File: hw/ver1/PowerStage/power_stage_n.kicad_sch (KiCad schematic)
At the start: 14 parts, among them Q2 Q_NMOS_DGS, Q6 Q_NMOS_DGS, U5 LTC7060

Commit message: Sync wip
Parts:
- removed D1: D_Schottky, symbol Device:D_Schottky
- removed Q2, Q6: Q_NMOS_DGS, symbol Device:Q_NMOS_DGS
- added D5: SS210, Diode_SMD:D_SMA, symbol Diode:SS210
- added Q10, Q2: MCAC80N10Y, Project Mosfets:TRANS_BSC076N06NS3-G, symbol ProjectMosfets:MCAC80N10Y
- C41: value C -> 200nF
- C45: value C -> 330nF
- L1: value L_Ferrite -> 3.3uH; Digikey (none) -> PQ2614BLA-3R3K-ND
- R53, R57: value R_US -> 10k
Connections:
- net GND: now also Q2.3 (S)
- net VCC: now also D5.2 (A)
- net VHIGH: now also Q10.1 (D)
- net at C11.2, L1.1, R53.1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: now also Q10.3 (S), Q2.1 (D)
- net at U5.11 (TG): now also Q10.2 (G)
- net at C11.1, U5.12 (BST): now also D5.1 (K)
- net at U5.8 (BG): now also Q2.2 (G)
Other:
- note added: "These components are sized to peak current load at 12v design limit from ltc7871.ipynb. Still need to validate other configurations."
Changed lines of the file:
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@@
+	)
+	(junction
+		(at 168.91 88.9)
+		(diameter 0)
+		(color 0 0 0 0)
 	)
 	(junction
@@
 		(color 0 0 0 0)
 	)
-	(junction
-		(at 168.91 88.9)
-		(diameter 0)
-		(color 0 0 0 0)
-	)
 	(no_connect
 		(at 133.35 76.2)
@@
 			(width 0)
 			(type default)
+		)
+	)
+	(text "These components are sized to peak current load at 12v design limit from ltc7871.ipynb.\nStill need to validate other configurations."
+		(exclude_from_sim no)
+		(at 169.926 37.846 0)
+		(effects
+			(font
+				(size 1.27 1.27)
+			)
 		)
 	)
@@
 			)
 		)
-		(property "Value" "L_Ferrite"
+		(property "Value" "3.3uH"
 			(at 193.04 79.248 90)
 			(effects
@@
 			)
 		)
-		(property "Datasheet" "~"
+		(property "Datasheet" "https://www.bourns.com/docs/Product-Datasheets/PQ2614.pdf"
 			(at 193.04 77.47 0)
 			(effects
@@
 		(property "Description" "Inductor with ferrite core"
 			(at 193.04 77.47 0)
+			(effects
+				(font
+					(size 1.27 1.27)
+				)
+				(hide yes)
+			)
+		)
+		(property "Digikey" "PQ2614BLA-3R3K-ND"
+			(at 193.548 81.28 90)
 			(effects
 				(font
@@
 	)
 	(symbol
-		(lib_id "Device:Q_NMOS_DGS")
-		(at 166.37 83.82 0)
+		(lib_id "ProjectMosfets:MCAC80N10Y")
+		(at 166.37 71.12 0)
 		(unit 1)
 		(exclude_from_sim no)
@@
 		(dnp no)
 		(fields_autoplaced yes)
-		(property "Reference" "Q6"
-			(at 172.72 82.5499 0)
+		(property "Reference" "Q10"
+			(at 172.72 69.8499 0)
 			(effects
 				(font
@@
 			)
 		)
-		(property "Value" "Q_NMOS_DGS"
-			(at 172.72 85.0899 0)
+		(property "Value" "MCAC80N10Y"
+			(at 172.72 72.3899 0)
 			(effects
 				(font
@@
 			)
 		)
-		(property "Footprint" ""
-			(at 171.45 81.28 0)
-			(effects
-				(font
-					(size 1.27 1.27)
-				)
-				(hide yes)
-			)
-		)
-		(property "Datasheet" "~"
-			(at 166.37 83.82 0)
+		(property "Footprint" "Project Mosfets:TRANS_BSC076N06NS3-G"
+			(at 171.45 68.58 0)
+			(effects
+				(font
+					(size 1.27 1.27)
+				)
+				(hide yes)
+			)
+		)
+		(property "Datasheet" "https://www.mccsemi.com/pdf/Products/MCAC80N10Y(DFN5060).pdf"
+			(at 166.37 71.12 0)
 			(effects
 				(font
@@
 		)
 		(property "Description" "N-MOSFET transistor, drain/gate/source"
-			(at 166.37 83.82 0)
+			(at 166.37 71.12 0)
+			(effects
+				(font
+					(size 1.27 1.27)
+				)
+				(hide yes)
+			)
+		)
+		(property "DigiKey" "353-MCAC80N10Y-TPCT-ND"
+			(at 166.37 71.12 0)
 			(effects
 				(font
@@
 		(pin "1"
 		)
+		(pin "2"
+		)
 		(pin "3"
-		)
-		(pin "2"
 		)
 		(instances
 			(project "IchnaeaV1"
 				(path "/1a8ad36a-4b76-4949-97c2-661f12a0b1d9/2acacade-9567-40f5-9827-bf22bd24fca6/ec98a9c6-939d-4e77-a0cb-de9e7d256244"
-					(reference "Q6")
+					(reference "Q10")
 					(unit 1)
 				)
 				(path "/1a8ad36a-4b76-4949-97c2-661f12a0b1d9/2acacade-9567-40f5-9827-bf22bd24fca6/fa9aff26-caf6-491a-a4dd-20eb067f1f07"
-					(reference "Q7")
+					(reference "Q11")
 					(unit 1)
 				)
 				(path "/1a8ad36a-4b76-4949-97c2-661f12a0b1d9/2acacade-9567-40f5-9827-bf22bd24fca6/9404991a-84cd-40d3-b41e-b6fd90033c77"
-					(reference "Q8")
+					(reference "Q12")
 					(unit 1)
 				)
 				(path "/1a8ad36a-4b76-4949-97c2-661f12a0b1d9/2acacade-9567-40f5-9827-bf22bd24fca6/951e871e-184d-412d-983e-cb08401577f3"
-					(reference "Q9")
+					(reference "Q13")
 					(unit 1)
 				)
@@
 			)
 		)
-		(property "Value" "R_US"
+		(property "Value" "10k"
 			(at 196.85 60.9599 0)
 			(effects
@@
 			)
 		)
-		(property "Value" "R_US"
+		(property "Value" "10k"
 			(at 180.34 60.96 90)
 			(effects
@@
 	)
 	(symbol
-		(lib_id "Device:C")
-		(at 185.42 54.61 0)
+		(lib_id "Diode:SS210")
+		(at 142.24 57.15 180)
 		(unit 1)
 		(exclude_from_sim no)
@@
 		(dnp no)
 		(fields_autoplaced yes)
+		(property "Reference" "D5"
+			(at 142.5575 50.8 0)
+			(effects
+				(font
+					(size 1.27 1.27)
+				)
+			)
+		)
+		(property "Value" "SS210"
+			(at 142.5575 53.34 0)
+			(effects
+				(font
+					(size 1.27 1.27)
+				)
+			)
+		)
+		(property "Footprint" "Diode_SMD:D_SMA"
+			(at 142.24 52.705 0)
+			(effects
+				(font
+					(size 1.27 1.27)
+				)
+				(hide yes)
+			)
+		)
+		(property "Datasheet" "https://www.wontop.com/uploadfiles/56/sort_excel/pdf/ss22.pdf"
+			(at 142.24 57.15 0)
+			(effects
+				(font
+					(size 1.27 1.27)
+				)
+				(hide yes)
+			)
+		)
+		(property "Description" "100V 2A Schottky Diode, SMA"
+			(at 142.24 57.15 0)
+			(effects
+				(font
+					(size 1.27 1.27)
+				)
+				(hide yes)
+			)
+		)
+		(property "LCSC" "C14996"
+			(at 142.24 57.15 0)
+			(effects
+				(font
+					(size 1.27 1.27)
+				)
+				(hide yes)
+			)
+		)
+		(pin "2"
+		)
+		(pin "1"
+		)
+		(instances
+			(project "IchnaeaV1"
+				(path "/1a8ad36a-4b76-4949-97c2-661f12a0b1d9/2acacade-9567-40f5-9827-bf22bd24fca6/ec98a9c6-939d-4e77-a0cb-de9e7d256244"
+					(reference "D5")
+					(unit 1)
+				)
+				(path "/1a8ad36a-4b76-4949-97c2-661f12a0b1d9/2acacade-9567-40f5-9827-bf22bd24fca6/fa9aff26-caf6-491a-a4dd-20eb067f1f07"
+					(reference "D6")
+					(unit 1)
+				)
+				(path "/1a8ad36a-4b76-4949-97c2-661f12a0b1d9/2acacade-9567-40f5-9827-bf22bd24fca6/9404991a-84cd-40d3-b41e-b6fd90033c77"
+					(reference "D7")
+					(unit 1)
+				)
+				(path "/1a8ad36a-4b76-4949-97c2-661f12a0b1d9/2acacade-9567-40f5-9827-bf22bd24fca6/951e871e-184d-412d-983e-cb08401577f3"
+					(reference "D8")
+					(unit 1)
+				)
+			)
+		)
+	)
+	(symbol
+		(lib_id "Device:C")
+		(at 185.42 54.61 0)
+		(mirror y)
+		(unit 1)
+		(exclude_from_sim no)
+		(in_bom yes)
+		(on_board yes)
+		(dnp no)
 		(property "Reference" "C41"
-			(at 189.23 53.3399 0)
+			(at 181.61 53.3399 0)
 			(effects
 				(font
@@
 			)
 		)
-		(property "Value" "C"
-			(at 189.23 55.8799 0)
+		(property "Value" "200nF"
+			(at 181.61 55.8799 0)
 			(effects
 				(font
@@
 		)
 		(property "Footprint" ""
-			(at 186.3852 58.42 0)
+			(at 184.4548 58.42 0)
 			(effects
 				(font
@@
 			)
 		)
-		(property "Value" "C"
+		(property "Value" "330nF"
 			(at 198.12 50.7999 0)
 			(effects
@@
 	)
 	(symbol
-		(lib_id "Device:D_Schottky")
-		(at 142.24 57.15 180)
-		(unit 1)
-		(exclude_from_sim no)
-		(in_bom yes)
-		(on_board yes)
-		(dnp no)
-		(fields_autoplaced yes)
-		(property "Reference" "D1"
-			(at 142.5575 50.8 0)
-			(effects
-				(font
-					(size 1.27 1.27)
-				)
-			)
-		)
-		(property "Value" "D_Schottky"
-			(at 142.5575 53.34 0)
-			(effects
-				(font
-					(size 1.27 1.27)
-				)
-			)
-		)
-		(property "Footprint" ""
-			(at 142.24 57.15 0)
-			(effects
-				(font
-					(size 1.27 1.27)
-				)
-				(hide yes)
-			)
-		)
-		(property "Datasheet" "~"
-			(at 142.24 57.15 0)
-			(effects
-				(font
-					(size 1.27 1.27)
-				)
-				(hide yes)
-			)
-		)
-		(property "Description" "Schottky diode"
-			(at 142.24 57.15 0)
-			(effects
-				(font
-					(size 1.27 1.27)
-				)
-				(hide yes)
-			)
-		)
-		(pin "1"
-		)
-		(pin "2"
-		)
-		(instances
-			(project "IchnaeaV1"
-				(path "/1a8ad36a-4b76-4949-97c2-661f12a0b1d9/2acacade-9567-40f5-9827-bf22bd24fca6/ec98a9c6-939d-4e77-a0cb-de9e7d256244"
-					(reference "D1")
-					(unit 1)
-				)
-				(path "/1a8ad36a-4b76-4949-97c2-661f12a0b1d9/2acacade-9567-40f5-9827-bf22bd24fca6/fa9aff26-caf6-491a-a4dd-20eb067f1f07"
-					(reference "D2")
-					(unit 1)
-				)
-				(path "/1a8ad36a-4b76-4949-97c2-661f12a0b1d9/2acacade-9567-40f5-9827-bf22bd24fca6/9404991a-84cd-40d3-b41e-b6fd90033c77"
-					(reference "D3")
-					(unit 1)
-				)
-				(path "/1a8ad36a-4b76-4949-97c2-661f12a0b1d9/2acacade-9567-40f5-9827-bf22bd24fca6/951e871e-184d-412d-983e-cb08401577f3"
-					(reference "D4")
-					(unit 1)
-				)
-			)
-		)
-	)
-	(symbol
-		(lib_id "Device:Q_NMOS_DGS")
-		(at 166.37 71.12 0)
+		(lib_id "ProjectMosfets:MCAC80N10Y")
+		(at 166.37 83.82 0)
 		(unit 1)
 		(exclude_from_sim no)
@@
 		(fields_autoplaced yes)
 		(property "Reference" "Q2"
-			(at 172.72 69.8499 0)
+			(at 172.72 82.5499 0)
 			(effects
 				(font
@@
 			)
 		)
-		(property "Value" "Q_NMOS_DGS"
-			(at 172.72 72.3899 0)
+		(property "Value" "MCAC80N10Y"
+			(at 172.72 85.0899 0)
 			(effects
 				(font
@@
 			)
 		)
-		(property "Footprint" ""
-			(at 171.45 68.58 0)
-			(effects
-				(font
-					(size 1.27 1.27)
-				)
-				(hide yes)
-			)
-		)
-		(property "Datasheet" "~"
-			(at 166.37 71.12 0)
+		(property "Footprint" "Project Mosfets:TRANS_BSC076N06NS3-G"
+			(at 171.45 81.28 0)
+			(effects
+				(font
+					(size 1.27 1.27)
+				)
+				(hide yes)
+			)
+		)
+		(property "Datasheet" "https://www.mccsemi.com/pdf/Products/MCAC80N10Y(DFN5060).pdf"
+			(at 166.37 83.82 0)
 			(effects
 				(font
@@
 		)
 		(property "Description" "N-MOSFET transistor, drain/gate/source"
-			(at 166.37 71.12 0)
+			(at 166.37 83.82 0)
+			(effects
+				(font
+					(size 1.27 1.27)
+				)
+				(hide yes)
+			)
+		)
+		(property "DigiKey" "353-MCAC80N10Y-TPCT-ND"
+			(at 166.37 83.82 0)
 			(effects
 				(font
@@
 		(pin "1"
 		)
+		(pin "2"
+		)
 		(pin "3"
 		)
-		(pin "2"
-		)
 		(instances

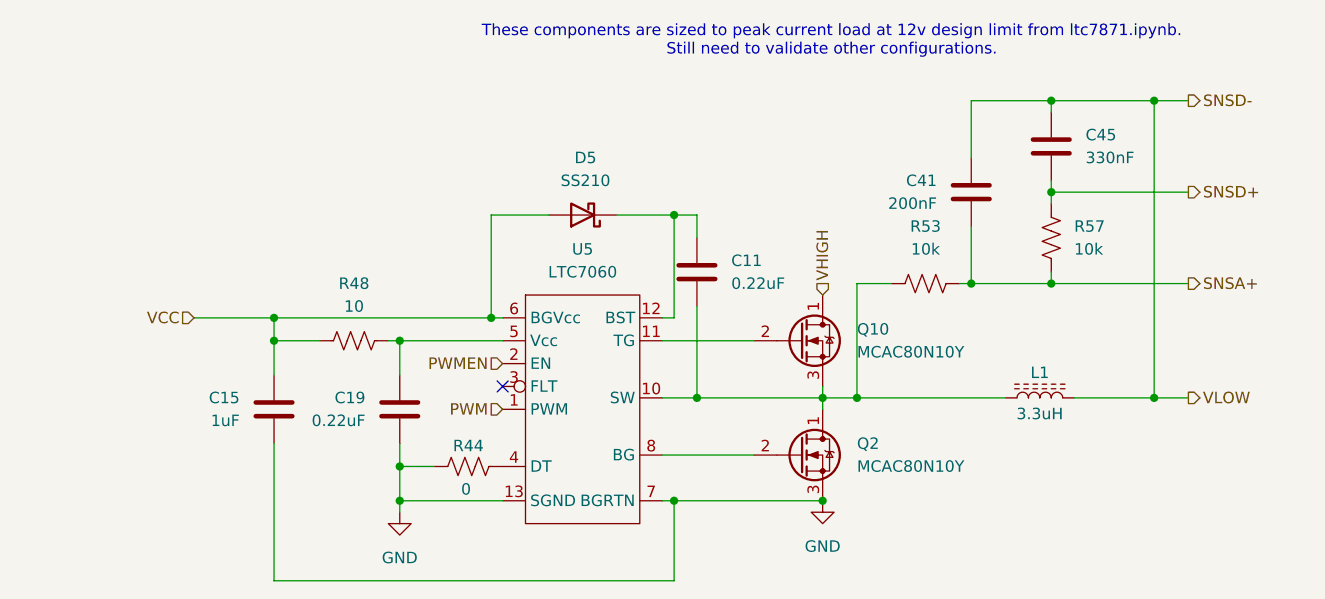
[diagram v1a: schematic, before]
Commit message: Do some parameterized designs and SPICE simulations with the LTC7871.
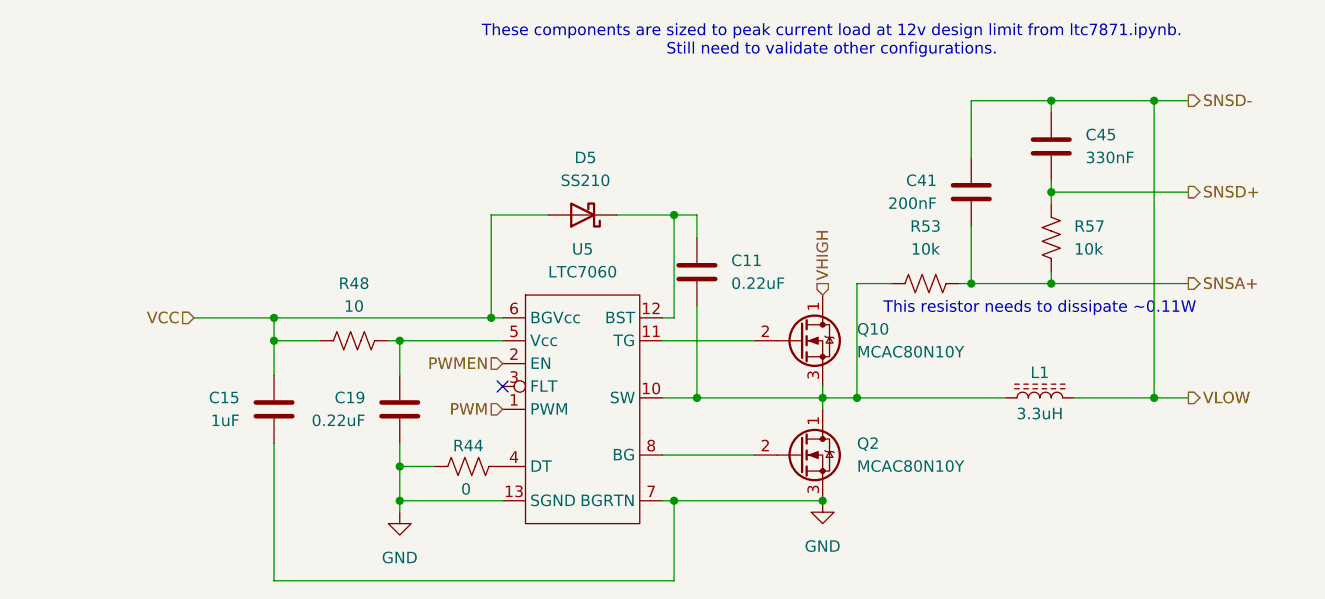
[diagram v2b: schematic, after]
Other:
- note added: "This resistor needs to dissipate ~0.11W"
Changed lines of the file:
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@@
+		)
+	)
+	(text "This resistor needs to dissipate ~0.11W"
+		(exclude_from_sim no)
+		(at 193.04 67.564 0)
+		(effects
+			(font
+				(size 1.27 1.27)
+			)
 		)
 	)

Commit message: Save lunchtime work
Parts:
- added C59: 2uF, symbol Device:C
- C41: value 200nF -> 100nF
- C45: value 330nF -> 470nF
- L1: value 3.3uH -> 4.7uH
- R53, R57: value 10k -> 6.2k
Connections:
- net GND: now also C59.2
- net SNSD-: now also C59.1
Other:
- note added: "This resistor needs to dissipate ~0.25W"
- note removed: "These components are sized to peak current load at 12v design limit from ltc7871.ipynb. Still need to validate other configurations."
- note removed: "This resistor needs to dissipate ~0.11W"

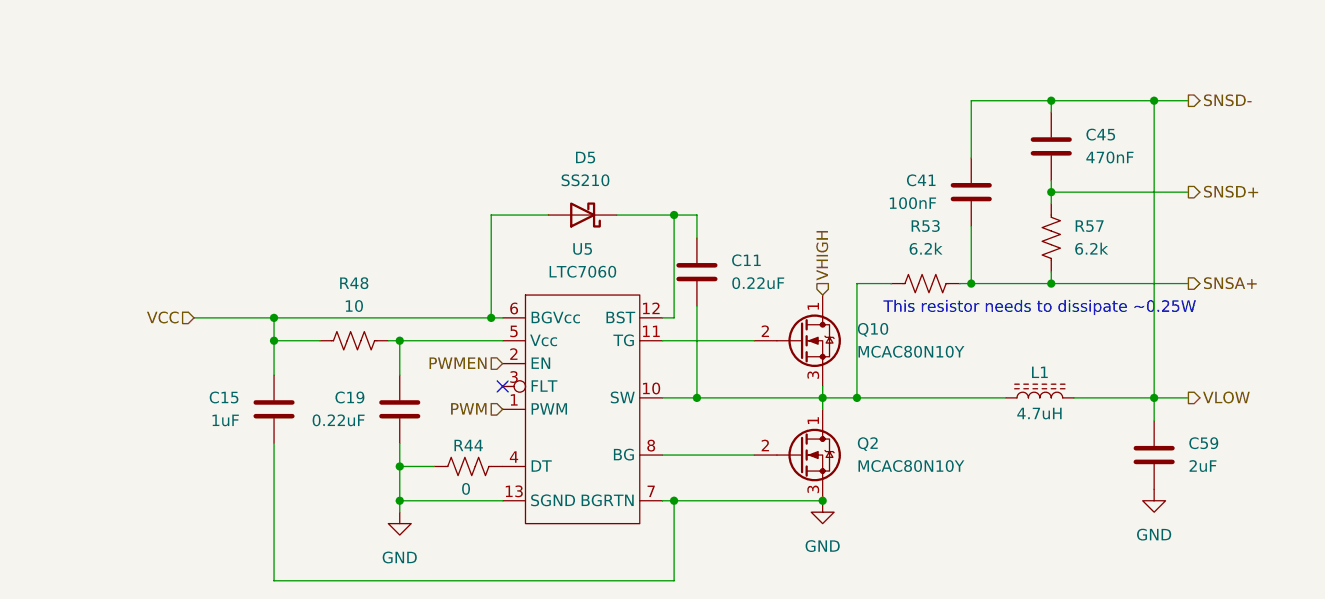
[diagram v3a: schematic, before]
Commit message: Add component part numbers for ordering. Resolve footprints.
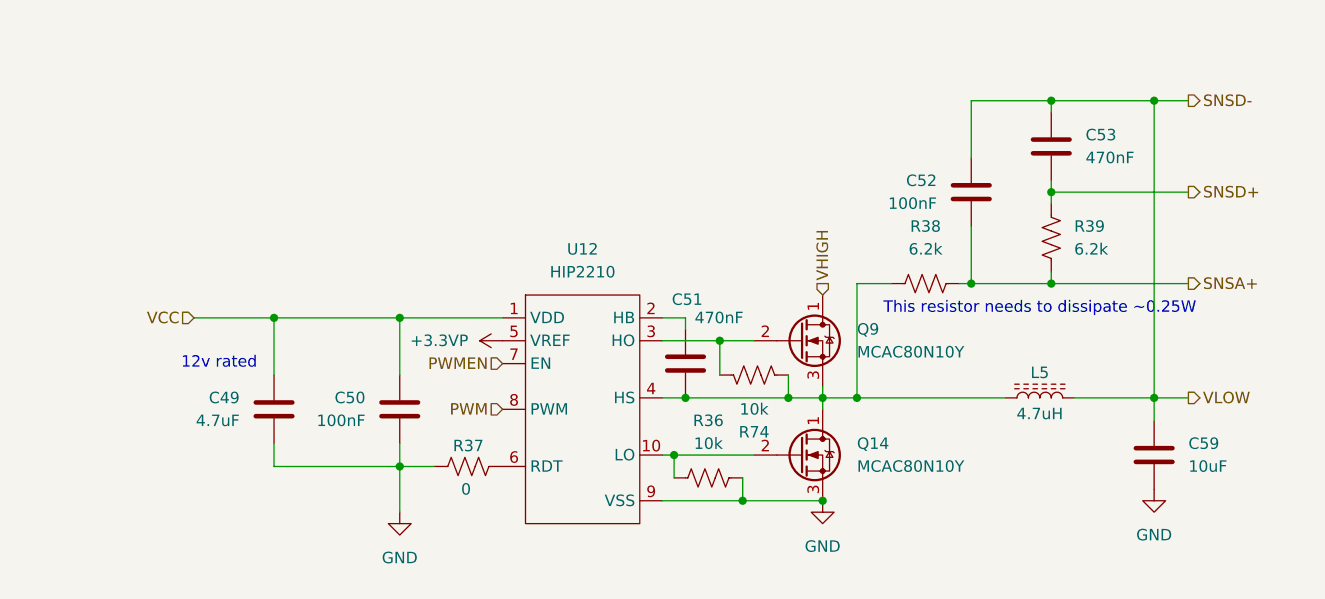
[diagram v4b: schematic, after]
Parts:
- removed D5: SS210, Diode_SMD:D_SMA, symbol Diode:SS210
- removed R48: 10, symbol Device:R_US
- removed U5: LTC7060, Package_SO:MSOP-12-1EP_3x4mm_P0.65mm_EP1.65x2.85mm_ThermalVias, symbol GateDrivers:LTC7060
- added R36, R74: 10k, Resistor_SMD:R_0603_1608Metric, symbol Device:R_US
- added U12: HIP2210, Package_DFN_QFN:TDFN-10-1EP_2x3mm_P0.5mm_EP0.9x2mm_ThermalVias, symbol GateDrivers:HIP2210
- C49: renamed from C15; value 1uF -> 4.7uF; footprint (none) -> Capacitor_SMD:C_0603_1608Metric; Digikey (none) -> N/A; LCSC (none) -> C19666
- C50: renamed from C19; value 0.22uF -> 100nF; footprint (none) -> Capacitor_SMD:C_0603_1608Metric; Digikey (none) -> N/A; LCSC (none) -> C14663
- C51: renamed from C11; value 0.22uF -> 470nF; footprint (none) -> Capacitor_SMD:C_0603_1608Metric; Digikey (none) -> N/A; LCSC (none) -> C1623
- C52: renamed from C41; footprint (none) -> Capacitor_SMD:C_0603_1608Metric; Digikey (none) -> N/A; LCSC (none) -> C14663
- C53: renamed from C45; footprint (none) -> Capacitor_SMD:C_0603_1608Metric; Digikey (none) -> N/A; LCSC (none) -> C1623
- C59: value 2uF -> 10uF; footprint (none) -> Capacitor_SMD:C_1210_3225Metric_Pad1.33x2.70mm_HandSolder; Digikey (none) -> 445-CGA6P1X7R1N106M250ACCT-ND
- L5: renamed from L1; footprint (none) -> Inductors:Bournes_L_PQ2614BLA; LCSC (none) -> N/A
- Q14: renamed from Q2; DigiKey 353-MCAC80N10Y-TPCT-ND -> (none); Digikey (none) -> 353-MCAC80N10Y-TPCT-ND; LCSC (none) -> N/A
- Q9: renamed from Q10; DigiKey 353-MCAC80N10Y-TPCT-ND -> (none); Digikey (none) -> 353-MCAC80N10Y-TPCT-ND; LCSC (none) -> N/A
- R37: renamed from R44; footprint (none) -> Capacitor_SMD:C_0603_1608Metric; Digikey (none) -> N/A; LCSC (none) -> C21189
- R38: renamed from R53; footprint (none) -> Resistor_SMD:R_1206_3216Metric_Pad1.30x1.75mm_HandSolder; Digikey (none) -> 311-6.20KFRCT-ND; LCSC (none) -> N/A
- R39: renamed from R57; footprint (none) -> Resistor_SMD:R_0603_1608Metric; Digikey (none) -> N/A; LCSC (none) -> C4260
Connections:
- net GND: now also R36.1, U12.9 (VSS)
- net PWM: now also U12.8 (PWM)
- net PWMEN: now also U12.7 (EN)
- net VCC: now also C50.1, U12.1 (VDD)
- net at R37.2: now also U12.6 (RDT)
- net at C51.2, L5.1, Q14.1 (D)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: now also R74.1, U12.4 (HS)
- net at Q9.2 (G): now also R74.2, U12.3 (HO)
- net at C51.1: now also U12.2 (HB)
- net at Q14.2 (G): now also R36.2, U12.10 (LO)
- new net +3.3VP: U12.5 (VREF)
- no-connect marks 1 -> 0
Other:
- note added: "12v rated"
- moved on the sheet: C51

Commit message: Sync some start to the PCB design
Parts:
- Q1: renamed from Q9; footprint Project Mosfets:TRANS_BSC076N06NS3-G -> Mosfets:TRANS_BSC076N06NS3-G
- Q2: renamed from Q14; footprint Project Mosfets:TRANS_BSC076N06NS3-G -> Mosfets:TRANS_BSC076N06NS3-G
- R1: renamed from R37; footprint Capacitor_SMD:C_0603_1608Metric -> Resistor_SMD:R_0603_1608Metric
- renumbered C49 to C1, C50 to C2, C51 to C3, C52 to C4, C53 to C5, C59 to C6, L5 to L1, R36 to R2, R74 to R3, R38 to R4, R39 to R5, U12 to U6
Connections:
- net GND: now also U6.11 (EPAD)
